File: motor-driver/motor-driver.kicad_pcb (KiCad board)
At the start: 4 copper layers, 56 x 85.4 mm, 123 parts, among them J1 10103594-0001LF, J2 SM03B-SRSS-TB, J3 XT60PW-F, J4 B2B-PH-SM4-TB, J5 S4B-XH-A, U1 PAD, U10 W25Q128JVS, U12 NCP1117ST33T3G, U13 RP2350B, U14 LM397, U15 LM397, U16 LM397, U17 FAN7388, U19 INA240A1PWR, U20 INA240A1PWR, U21 INA240A1PWR, Y1 ABM8-272-T3

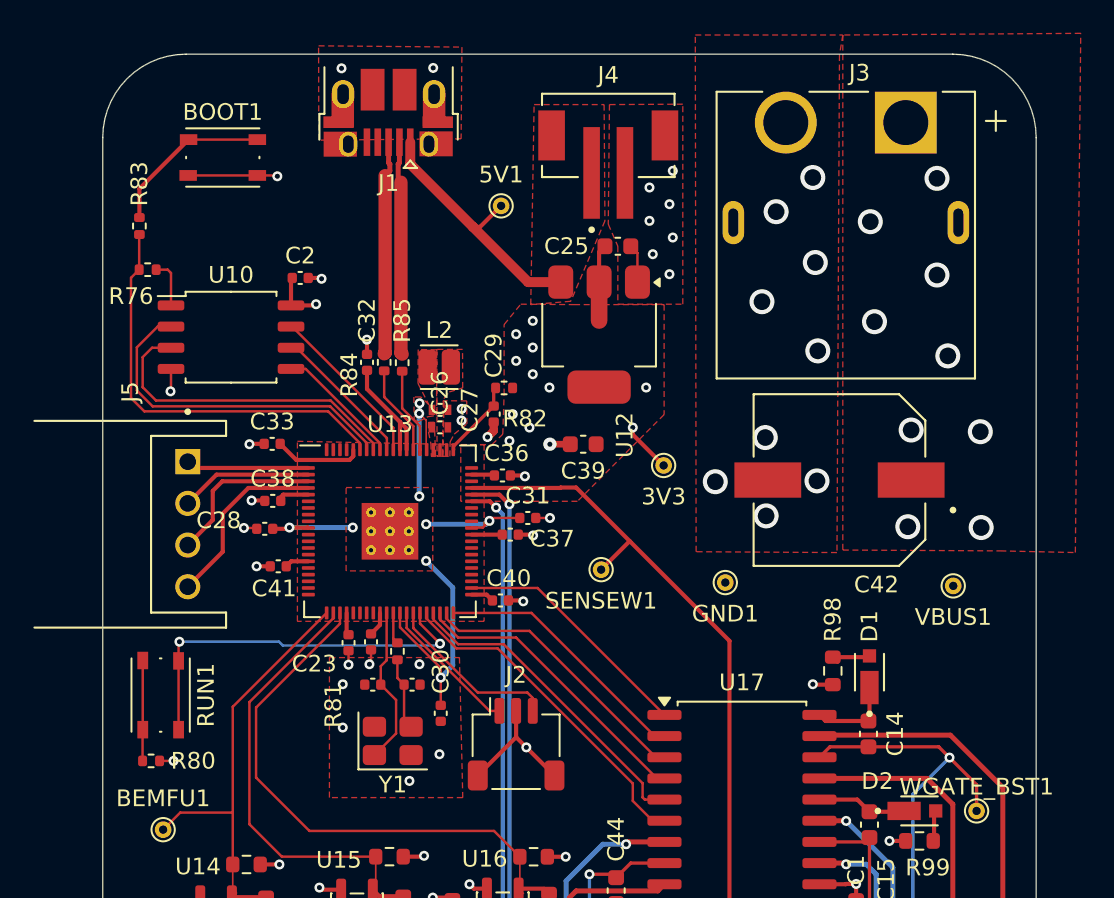
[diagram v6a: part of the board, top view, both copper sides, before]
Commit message: changed push buttons and zone clearances
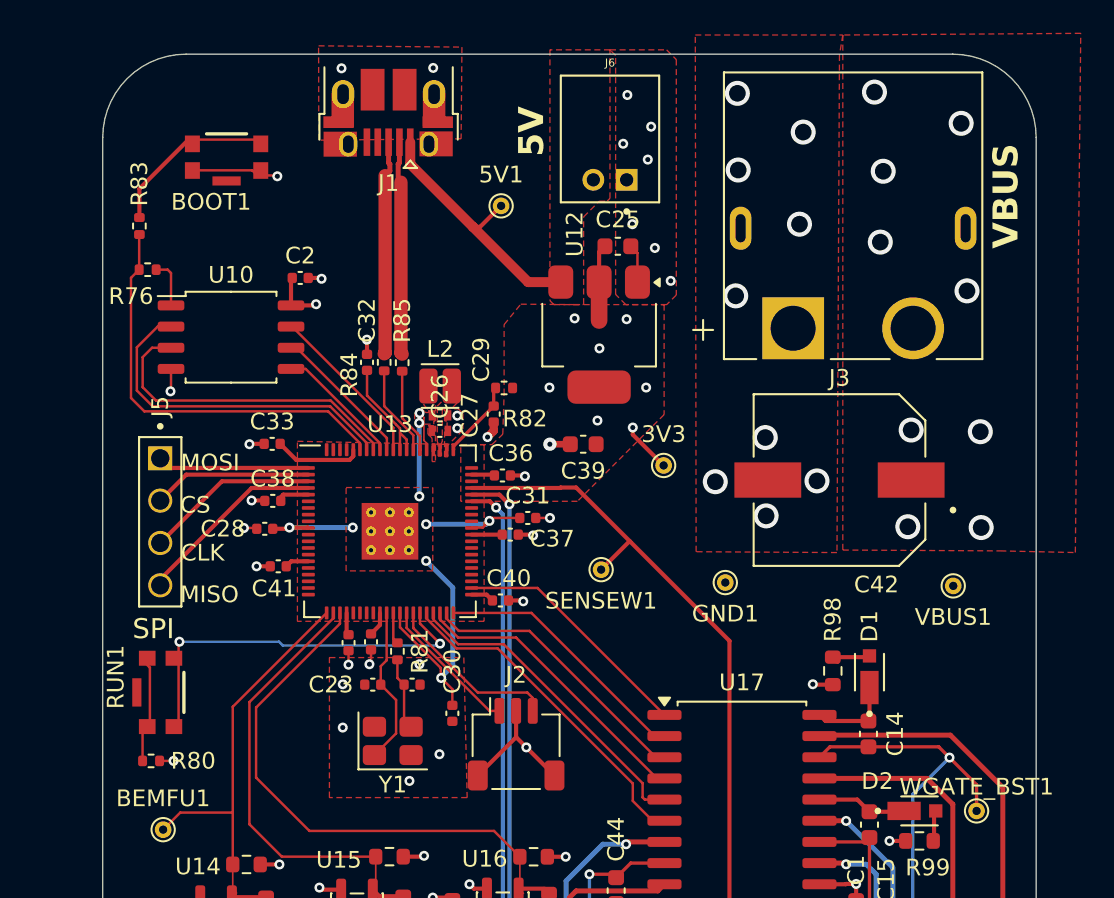
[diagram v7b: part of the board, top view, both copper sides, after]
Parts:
- removed J4: B2B-PH-SM4-TB, B2B-PH-SM4-TB:JST_B2B-PH-SM4-TB
- added J6: S2B-PH-K-S_LF__SN_, S2B-PH-K:JST_S2B-PH-K-S_LF__SN_, F.Cu at (167.8, 39.2)
- BOOT1, RUN1: value 434133025816 -> KMR221GLFS; footprint Button_Switch_SMD:SW_Push_1P1T_NO_Vertical_Wuerth_434133025816 -> KMR221GLFS:SW_KMR221GLFS
- C1: value 1uF -> 1u
- C14, C15, C3, C4, C44, C5: value 0.1uF -> 0.1u
- C42: value 330uF -> 330u
- J5: value S4B-XH-A -> 61300411121; footprint S4B-XH-A:JST_S4B-XH-A -> 61300411121:WURTH_61300411121
- L2: value AOTA-B201610S3R3-101-T -> 3.3u
- MOSFET1, MOSFET10, MOSFET2, MOSFET7, MOSFET8, MOSFET9: value AON6512 -> NMOS
- R100, R98, R99: value 50 -> 33
- moved J3 12.3 mm to (182.4, 48.1), turned to 180 degrees
- moved J5 4.05 mm to (140.8, 59.8)
- moved L2 1.13 mm to (157.6, 51.6)
- moved C30 0.70 mm to (158.4, 71.2)
- moved C27 0.33 mm to (157.6, 53.4)
- moved BOOT1 0.23 mm to (144.8, 37.9)
- moved C26 0.21 mm to (157.6, 54.3)
- moved RUN1 0.16 mm to (140.9, 70.0)
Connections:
- J3 pad 1: V_BUS -> GND
- J3 pad 2: GND -> V_BUS
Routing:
- net /RP2350/MOSI: track 7.39 -> 9.13 mm
- net /RP2350/CS: track 7.95 -> 9.53 mm
- net 3V3: track 64.4 -> 63.7 mm, vias 18 -> 14
- net /RP2350/SCLK: track 9.85 -> 10.4 mm
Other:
- board text added: "5V"
- board text added: "CLK"
- board text added: "CS"
- board text added: "MISO"
- board text added: "MOSI"
- board text added: "SPI"
- board text added: "VBUS"

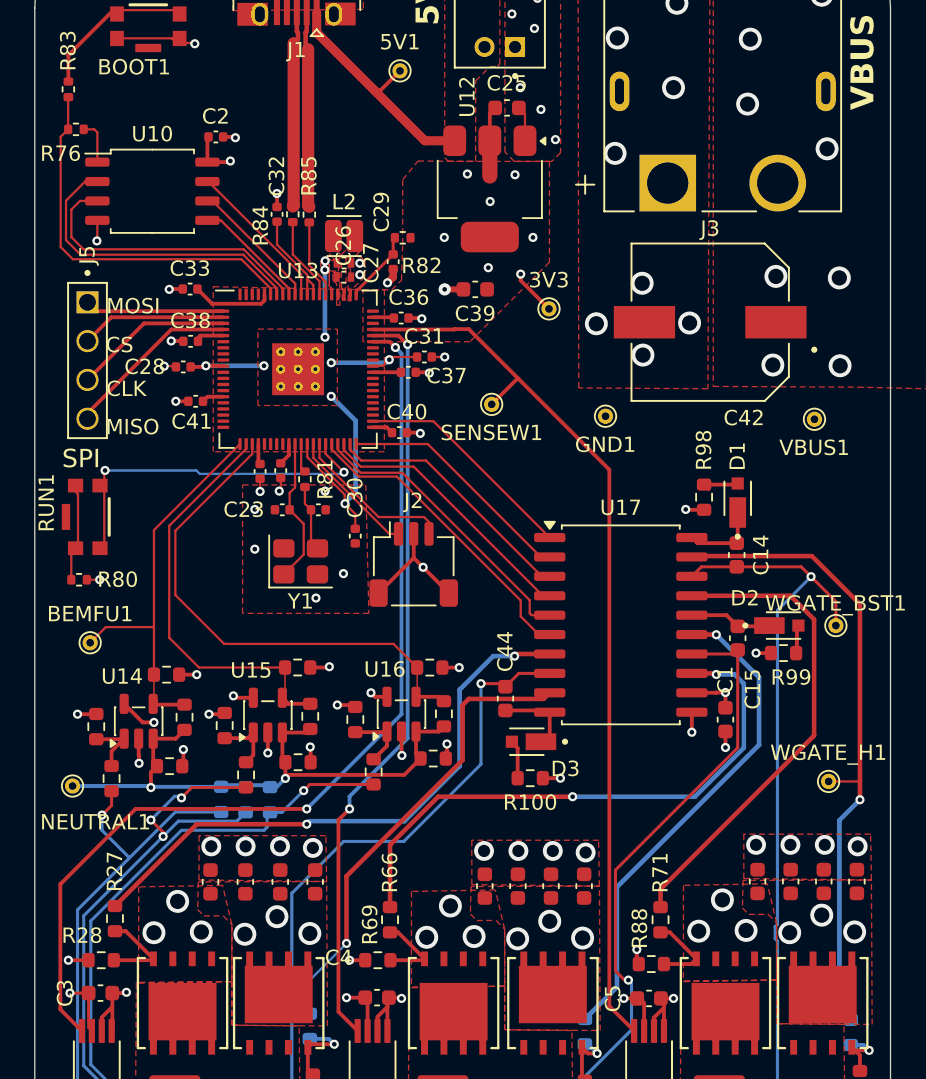
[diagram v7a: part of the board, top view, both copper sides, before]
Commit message: reoriented parts
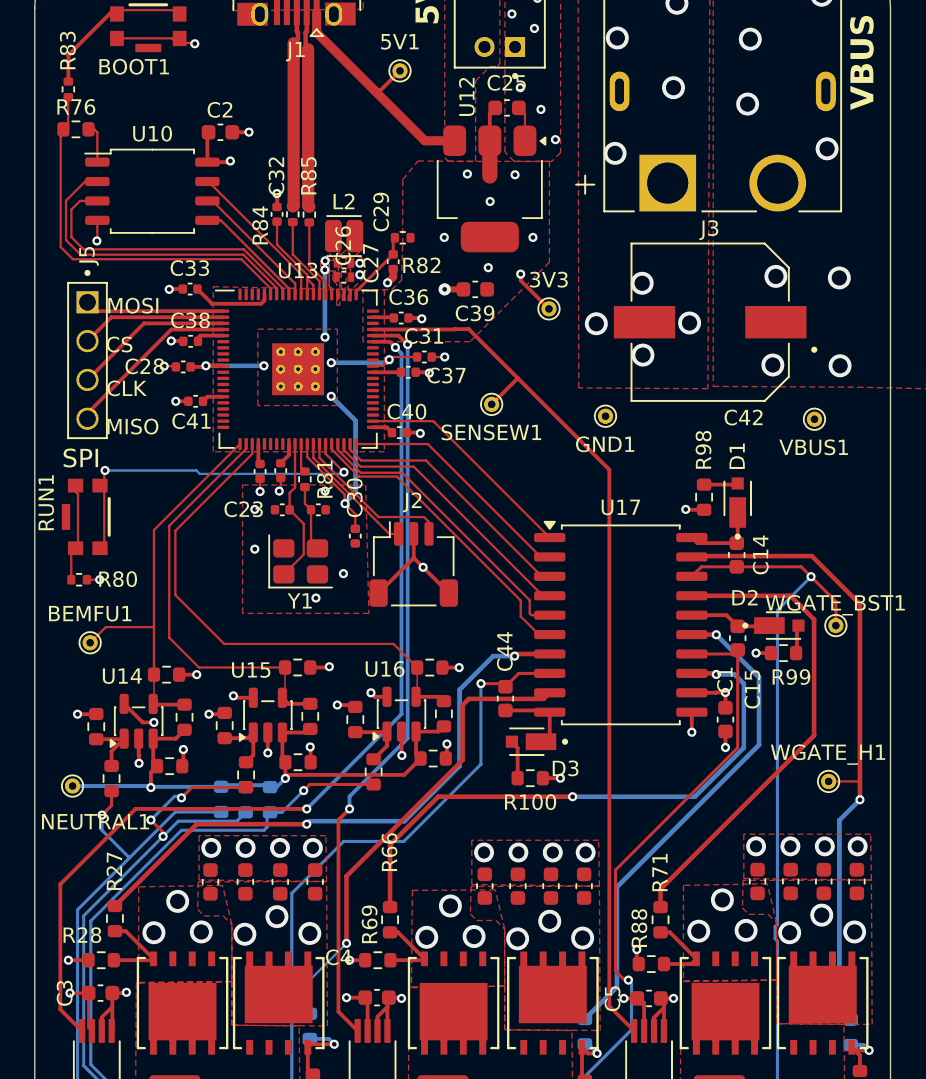
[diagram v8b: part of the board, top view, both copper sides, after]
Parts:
- C2: footprint Capacitor_SMD:C_0402_1005Metric -> Capacitor_SMD:C_0603_1608Metric
- R27, R6, R66, R67, R71, R86: value 22 -> 0
- R76: footprint Resistor_SMD:R_0402_1005Metric -> Resistor_SMD:R_0603_1608Metric
- moved C2 0.43 mm to (149.6, 44.8)
